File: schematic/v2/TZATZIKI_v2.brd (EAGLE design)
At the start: 41 x 50 mm, 4 parts, among them J1 2X20-CHIP-HEADERS2X20CHIP_OFF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, J2 USD-SDIO-SOCKET

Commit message: added fourway version
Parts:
- removed J2: USD-SDIO-SOCKET, JKW_CHIP:MICRO-SD-SOCKET-SDIO
- added POWER_USB: USBUSB-MICROB-SMT-DIP, Spark:USB-MICROB-SMT-DIP
- added SDIO_BOT, SDIO_TOP, SPI_BOT, SPI_TOP: USD-SDIO-SOCKET, JKW_CHIP:MICRO-SD-SOCKET-SDIO
- moved U$2 51.2 mm to (37.5, 17.3), turned to 0 degrees
- moved U$1 46.0 mm to (27.7, 17.5), turned to 0 degrees
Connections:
- removed net N$1: J1.CHG-IN
- new net N$11: J1.CSIPCK, SPI_BOT.CD/DAT3, SPI_TOP.CD/DAT3
- new net N$12: J1.CSIHSYNC, SPI_BOT.CMD, SPI_TOP.CMD
- new net N$13: J1.CSIVSYNC, SPI_BOT.DAT0, SPI_TOP.DAT0
- new net N$14: J1.CSICK, SPI_BOT.CLK, SPI_TOP.CLK
- new net VOUT: J1.CHG-IN, POWER_USB.VBUS
- net GND: now also POWER_USB.GND, POWER_USB.MT1, POWER_USB.MT2, SDIO_BOT.CD1, SDIO_BOT.CD2, SDIO_BOT.GND, SDIO_BOT.GND1, SDIO_BOT.GND3, SDIO_BOT.GND@1, SDIO_BOT.GND@2, SDIO_TOP.CD1, SDIO_TOP.CD2, SDIO_TOP.GND, SDIO_TOP.GND1, SDIO_TOP.GND3, SDIO_TOP.GND@1, SDIO_TOP.GND@2, SPI_BOT.CD1, SPI_BOT.CD2, SPI_BOT.GND, SPI_BOT.GND1, SPI_BOT.GND3, SPI_BOT.GND@1, SPI_BOT.GND@2, SPI_TOP.CD1, SPI_TOP.CD2, SPI_TOP.GND, SPI_TOP.GND1, SPI_TOP.GND3, SPI_TOP.GND@1, SPI_TOP.GND@2; no longer J2.CD1, J2.CD2, J2.GND, J2.GND1, J2.GND3, J2.GND@1, J2.GND@2
- net N$10: now also SDIO_BOT.VDD, SDIO_TOP.VDD, SPI_BOT.VDD, SPI_TOP.VDD; no longer J2.VDD
- net N$2: now also SDIO_BOT.CD/DAT3, SDIO_TOP.CD/DAT3; no longer J2.CD/DAT3
- net N$3: now also SDIO_BOT.DAT0, SDIO_TOP.DAT0; no longer J2.DAT0
- net N$4: now also SDIO_BOT.CMD, SDIO_TOP.CMD; no longer J2.CMD
- net N$5: now also SDIO_BOT.CLK, SDIO_TOP.CLK; no longer J2.CLK
- net N$6: now also SDIO_BOT.DAT1, SDIO_TOP.DAT1; no longer J2.DAT1
- net N$9: now also SDIO_BOT.DAT2, SDIO_TOP.DAT2; no longer J2.DAT2
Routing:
- net N$9: track 24.3 -> 82.7 mm, vias 0 -> 2
- net N$2: track 29.1 -> 85.5 mm, vias 0 -> 4
- net N$13: track 0.00 -> 51.7 mm, vias 0 -> 1
- net GND: track 29.1 -> 80.8 mm, vias 0 -> 4
- net N$3: track 30.3 -> 79.2 mm
- net N$4: track 27.6 -> 76.5 mm, vias 0 -> 2
- net N$14: track 0.00 -> 42.4 mm, vias 0 -> 1
- net N$11: track 0.00 -> 41.6 mm, vias 0 -> 3
- net N$12: track 0.00 -> 38.6 mm, vias 0 -> 3
- net N$5: track 33.0 -> 62.9 mm, vias 0 -> 2
- net VOUT: track 0.00 -> 28.3 mm
- net N$6: track 35.8 -> 58.1 mm, vias 1 -> 2
- net N$10: track 39.8 -> 48.0 mm, vias 1 -> 2
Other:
- board text added: "JKW v0.1 2016"

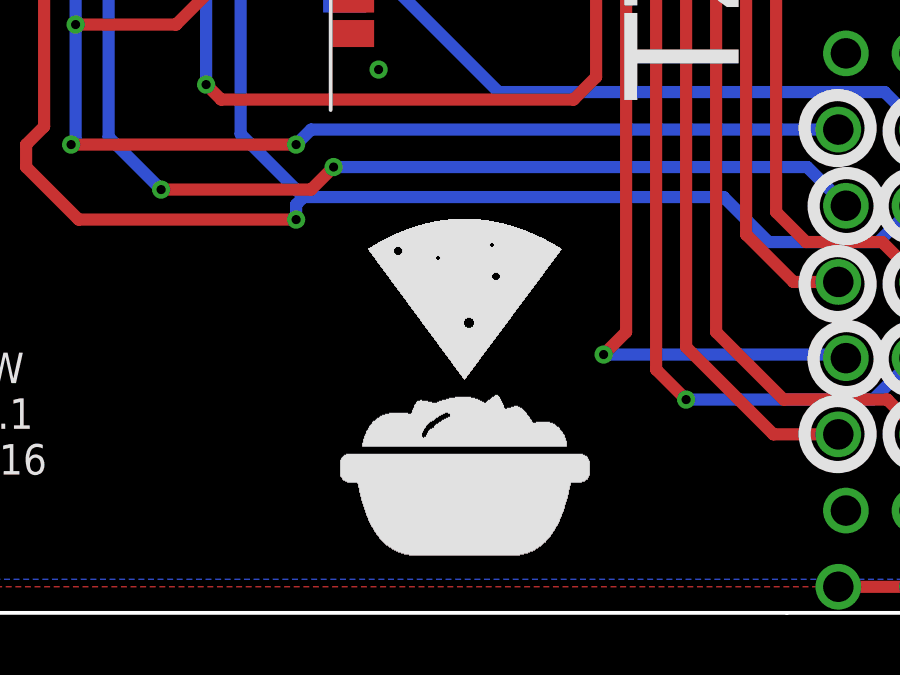
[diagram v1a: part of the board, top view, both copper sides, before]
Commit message: added v4 with card detect pin
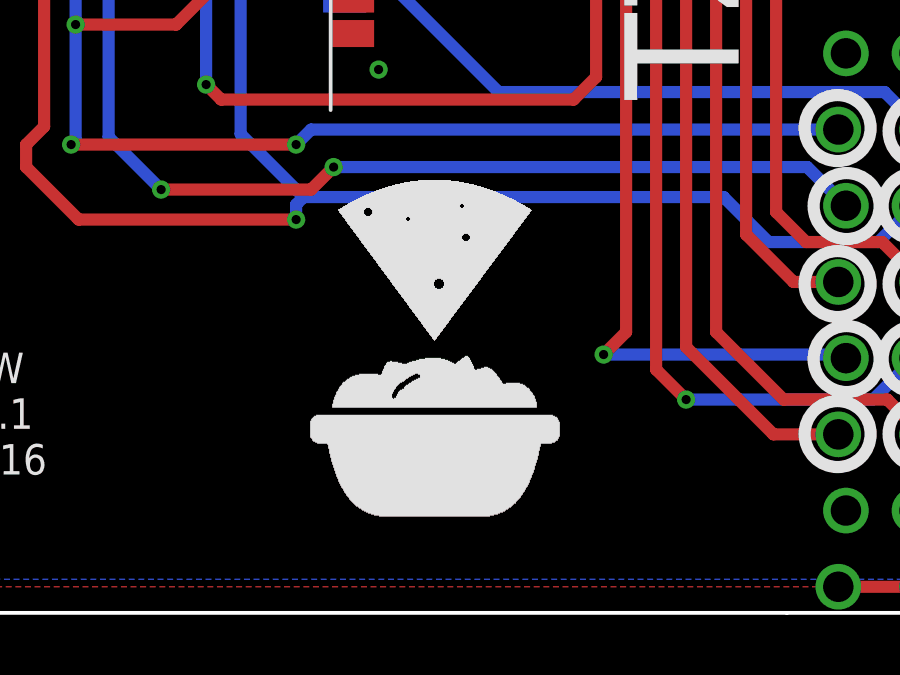
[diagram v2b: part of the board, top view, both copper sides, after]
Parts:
- moved U$1 1.64 mm to (26.7, 18.8)
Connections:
- new net N$1: J1.CSID7, SDIO_BOT.CD2, SDIO_TOP.CD2, SPI_BOT.CD2, SPI_TOP.CD2
- new net N$19: J1.CSID6, SDIO_BOT.CD1, SDIO_TOP.CD1, SPI_BOT.CD1, SPI_TOP.CD1
- net GND: no longer SDIO_BOT.CD1, SDIO_BOT.CD2, SDIO_TOP.CD1, SDIO_TOP.CD2, SPI_BOT.CD1, SPI_BOT.CD2, SPI_TOP.CD1, SPI_TOP.CD2
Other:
- board text added: "Ordered 2016/08/08 OSH"
